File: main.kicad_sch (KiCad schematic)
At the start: 18 parts, among them J1 RPi UART Debug LEDs, J2 mini iso blue, J3 LCD power, P1 Conn_02x20_Odd_Even, U7 DS3231MZ

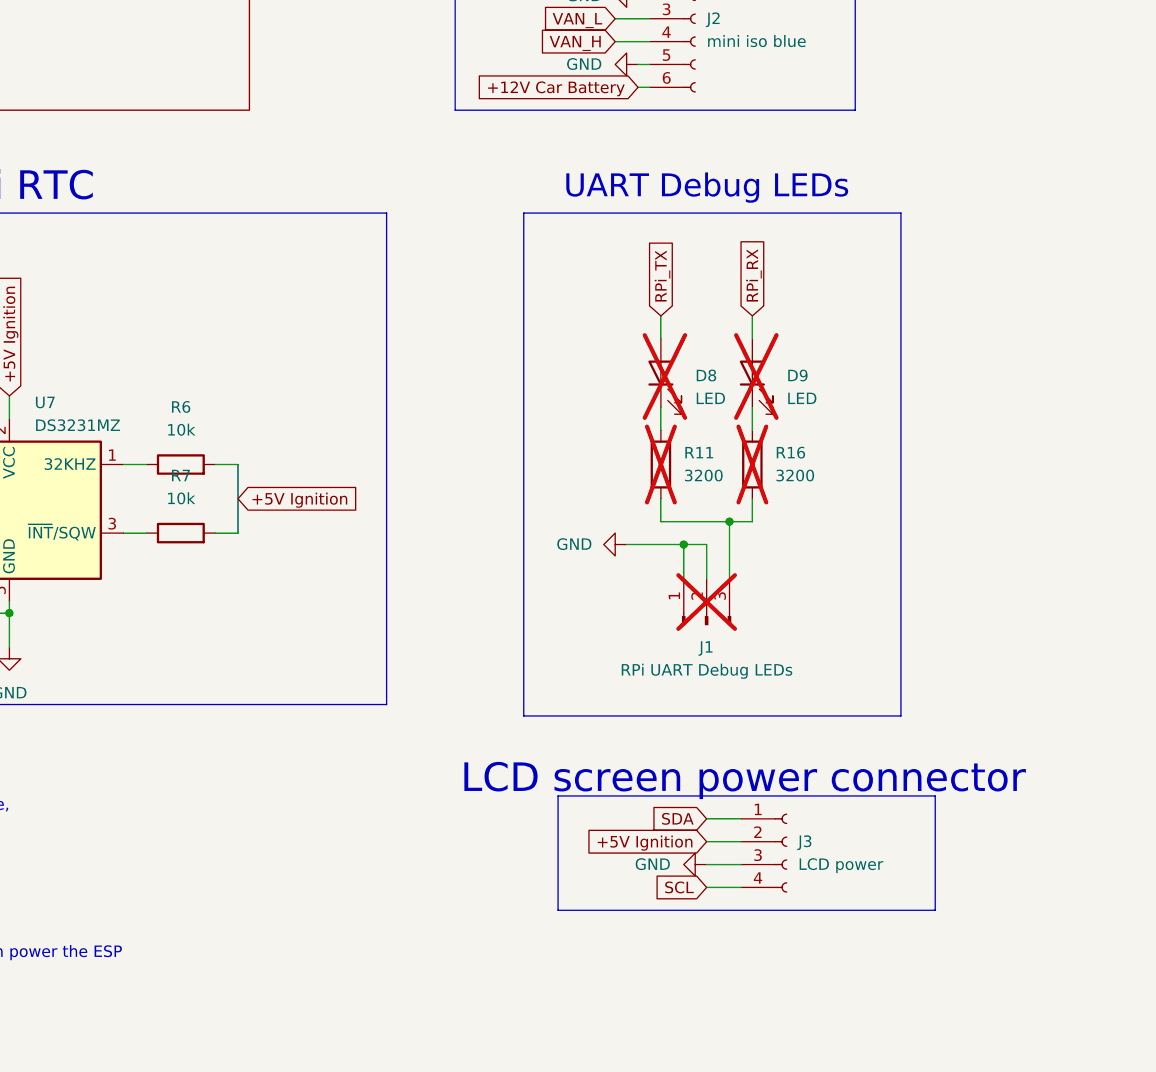
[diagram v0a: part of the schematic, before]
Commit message: implemented the changes from 'Board defects'
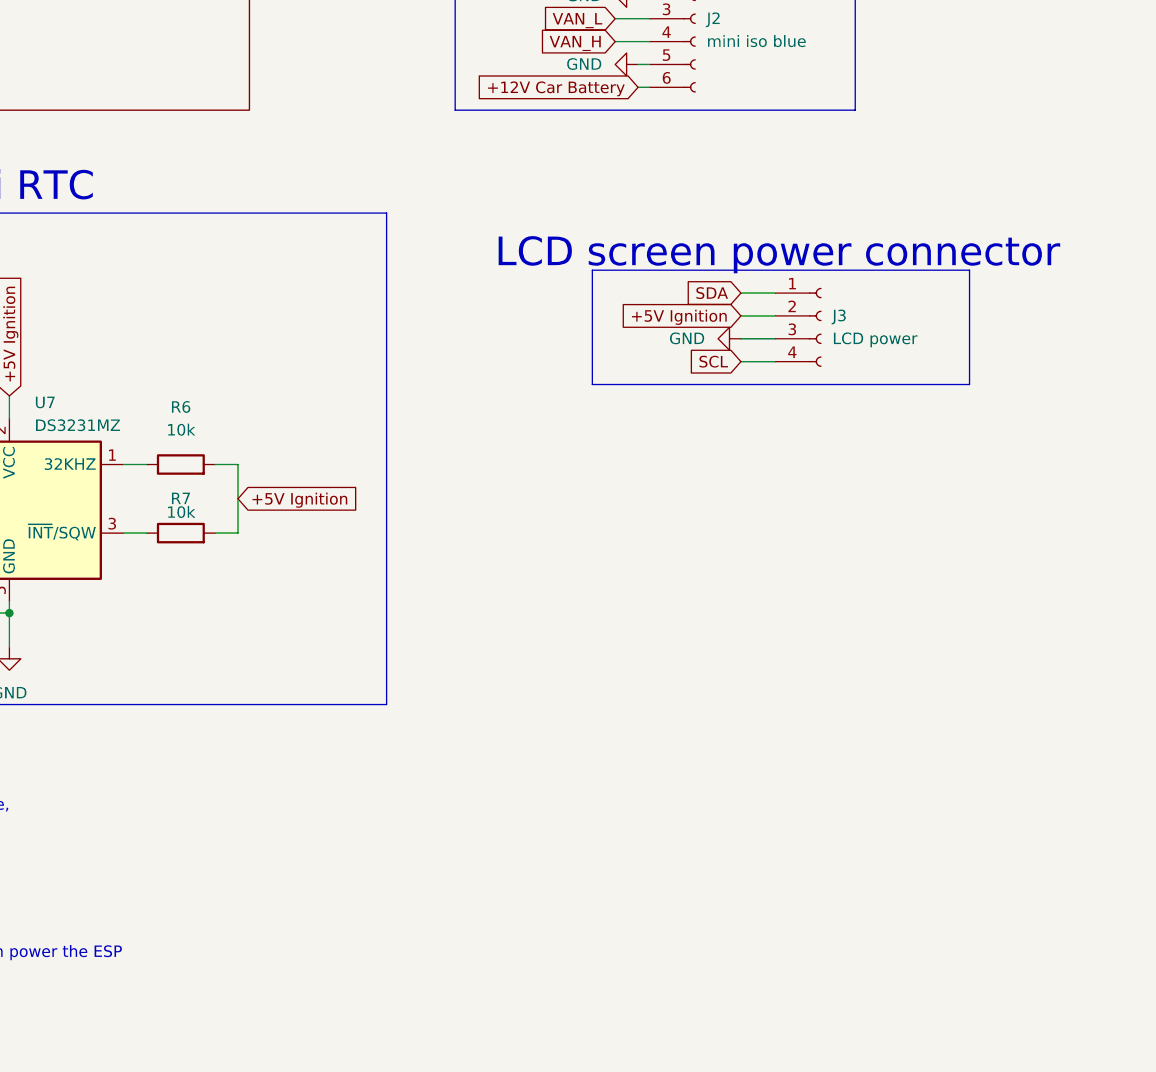
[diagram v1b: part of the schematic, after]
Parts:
- removed D8, D9: LED, LED_SMD:LED_0402_1005Metric, symbol Device:LED
- removed J1: RPi UART Debug LEDs, Connector_PinHeader_2.54mm:PinHeader_1x03_P2.54mm_Vertical, symbol Connector:Conn_01x03_Pin
- removed R11, R16: 3200, Resistor_SMD:R_0805_2012Metric, symbol Device:R
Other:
- note removed: "UART Debug LEDs"
- moved on the sheet: J3

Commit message: 2 layer PCB
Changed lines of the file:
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@@
+	)
+	(junction
+		(at 83.82 88.9)
+		(diameter 1.016)
+		(color 0 0 0 0)
+	)
+	(junction
+		(at 83.82 63.5)
+		(diameter 1.016)
+		(color 0 0 0 0)
+	)
+	(junction
+		(at 66.04 78.74)
+		(diameter 1.016)
+		(color 0 0 0 0)
+	)
+	(junction
+		(at 52.07 53.34)
+		(diameter 0)
+		(color 0 0 0 0)
 	)
 	(junction
@@
 	)
 	(junction
-		(at 83.82 88.9)
-		(diameter 1.016)
-		(color 0 0 0 0)
-	)
-	(junction
-		(at 83.82 63.5)
-		(diameter 1.016)
-		(color 0 0 0 0)
-	)
-	(junction
-		(at 66.04 78.74)
-		(diameter 1.016)
-		(color 0 0 0 0)
-	)
-	(junction
-		(at 52.07 53.34)
-		(diameter 0)
-		(color 0 0 0 0)
-	)
-	(junction
 		(at 123.19 128.27)
 		(diameter 0)
@@
 	(wire
 		(pts
+			(xy 62.23 39.37) (xy 52.07 39.37)
+		)
+		(stroke
+			(width 0)
+			(type default)
+		)
+	)
+	(wire
+		(pts
 			(xy 208.28 67.31) (xy 209.55 67.31)
 		)
@@
 	(wire
 		(pts
+			(xy 52.07 39.37) (xy 52.07 41.91)
+		)
+		(stroke
+			(width 0)
+			(type default)
+		)
+	)
+	(wire
+		(pts
 			(xy 153.67 119.38) (xy 151.13 119.38)
 		)
@@
 	(wire
 		(pts
+			(xy 62.23 48.26) (xy 62.23 63.5)
+		)
+		(stroke
+			(width 0)
+			(type default)
+		)
+	)
+	(wire
+		(pts
 			(xy 83.82 63.5) (xy 81.28 63.5)
 		)
@@
 	(wire
 		(pts
+			(xy 62.23 48.26) (xy 68.58 48.26)
+		)
+		(stroke
+			(width 0)
+			(type default)
+		)
+	)
+	(wire
+		(pts
 			(xy 66.04 78.74) (xy 66.04 96.52)
 		)
@@
 	(wire
 		(pts
-			(xy 52.07 41.91) (xy 62.23 41.91)
-		)
-		(stroke
-			(width 0)
-			(type default)
-		)
-	)
-	(wire
-		(pts
 			(xy 52.07 53.34) (xy 68.58 53.34)
 		)
@@
 	(wire
 		(pts
-			(xy 86.36 44.45) (xy 86.36 48.26)
+			(xy 86.36 33.02) (xy 86.36 48.26)
 		)
 		(stroke
@@
 	(wire
 		(pts
-			(xy 62.23 41.91) (xy 62.23 48.26)
+			(xy 62.23 39.37) (xy 62.23 48.26)
 		)
 		(stroke
@@
 	(wire
 		(pts
-			(xy 62.23 48.26) (xy 68.58 48.26)
-		)
-		(stroke
-			(width 0)
-			(type default)
-		)
-	)
-	(wire
-		(pts
 			(xy 86.36 48.26) (xy 81.28 48.26)
 		)
@@
 		)
 	)
-	(wire
-		(pts
-			(xy 62.23 48.26) (xy 62.23 63.5)
-		)
-		(stroke
-			(width 0)
-			(type default)
-		)
-	)
 	(global_label "+5V Ignition"
 		(shape input)
@@
 	(global_label "+5V Ignition"
 		(shape input)
-		(at 86.36 44.45 90)
+		(at 86.36 33.02 90)
 		(fields_autoplaced yes)
 		(effects
@@
 		)
 		(property "Intersheetrefs" "${INTERSHEET_REFS}"
-			(at 86.36 29.3955 90)
-			(effects
-				(font
+			(at 86.36 17.9655 90)
+			(effects
+				(font

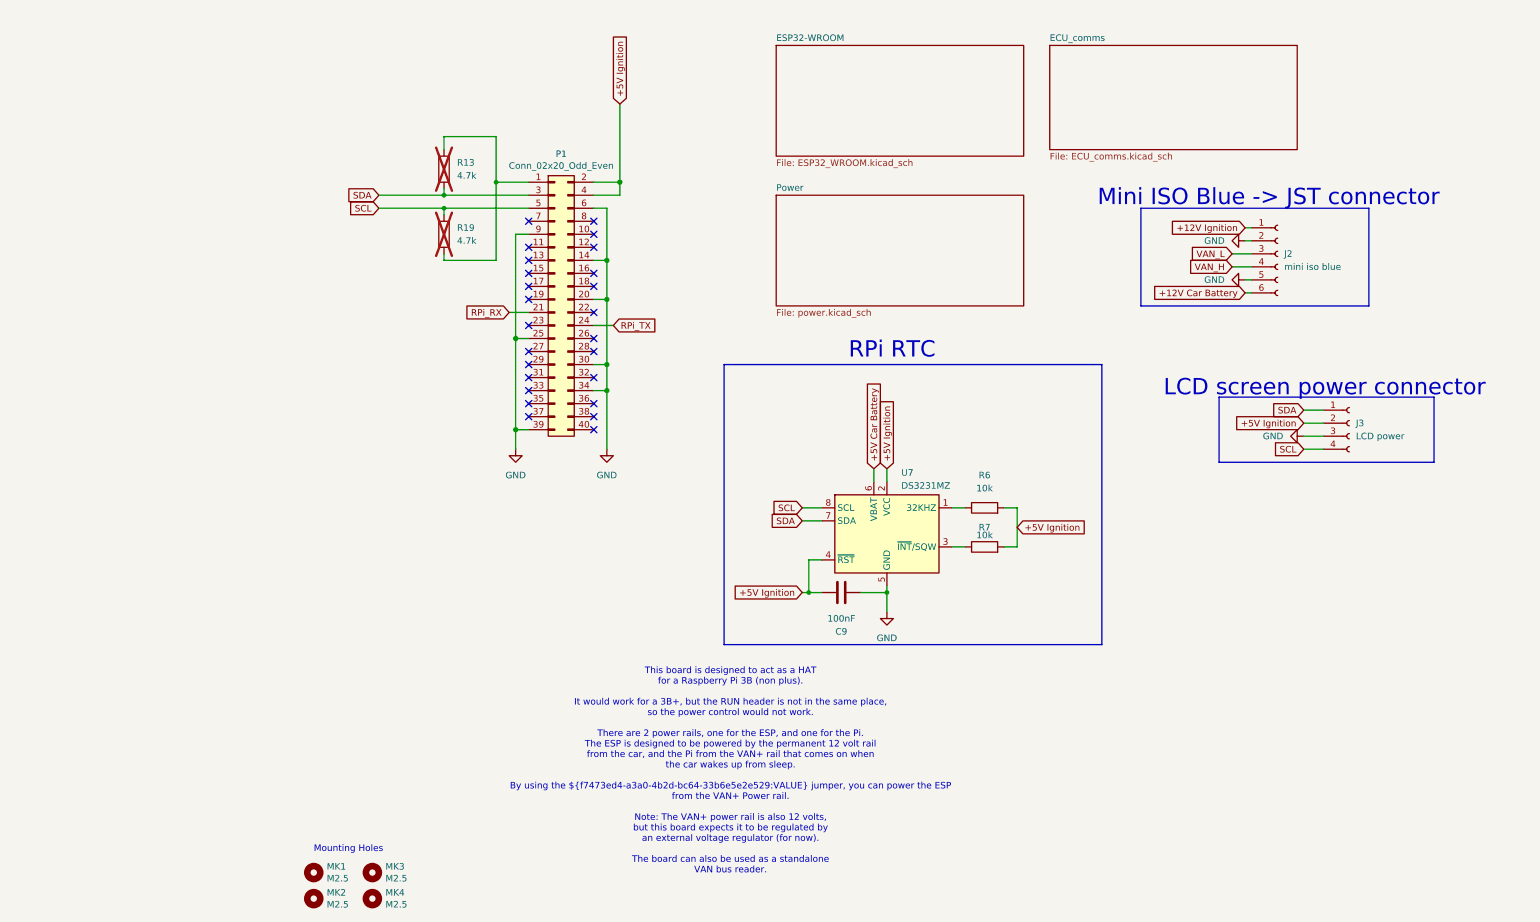
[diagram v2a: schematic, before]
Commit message: Change inductor type.
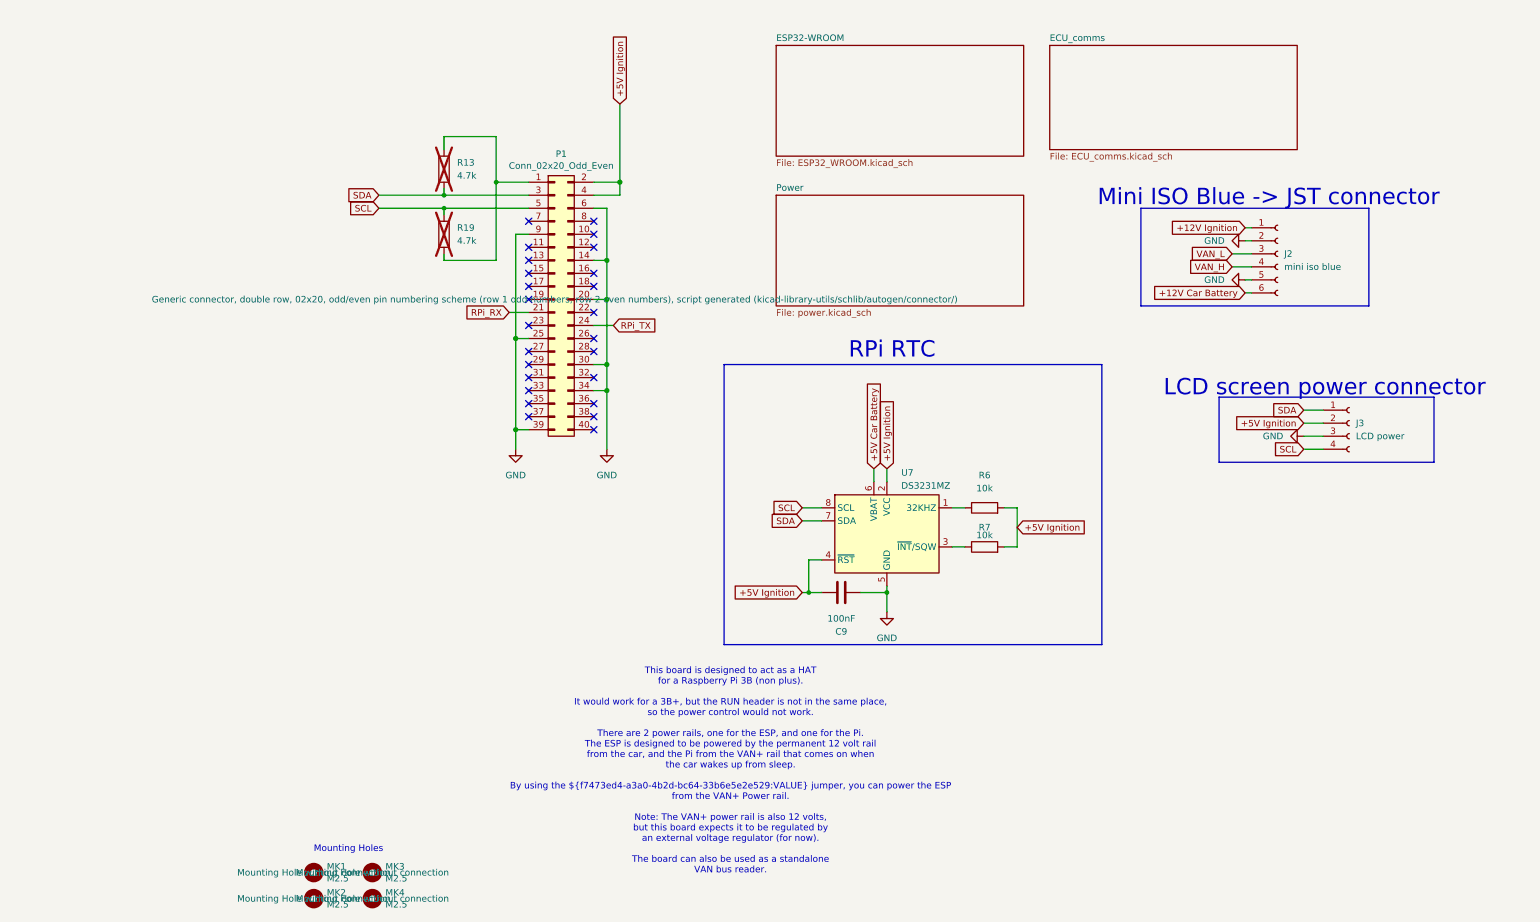
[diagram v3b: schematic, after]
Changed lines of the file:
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@@
 			)
 		)
-		(property "Description" ""
+		(property "Description" "Mounting Hole without connection"
 			(at 26.67 182.88 0)
 			(effects
@@
 			)
 		)
-		(property "Description" ""
+		(property "Description" "Mounting Hole without connection"
 			(at 38.1 182.88 0)
 			(effects
@@
 			)
 		)
-		(property "Description" ""
+		(property "Description" "Mounting Hole without connection"
 			(at 26.67 187.96 0)
 			(effects
@@
 			)
 		)
-		(property "Description" ""
+		(property "Description" "Mounting Hole without connection"
 			(at 38.1 187.96 0)
 			(effects
@@
 			)
 		)
-		(property "Description" ""
+		(property "Description" "Generic connector, double row, 02x20, odd/even pin numbering scheme (row 1 odd numbers, row 2 even numbers), script generated (kicad-library-utils/schlib/autogen/connector/)"
 			(at 73.66 71.12 0)
 			(effects

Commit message: Update bom values with actual chip names
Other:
- note removed: "This board is designed to act as a HAT for a Raspberry Pi 3B (non plus). It would work for a 3B+, but the RUN header is not in the same place, so the power control would not work. There are 2 power rails, one for the ESP, and one for the Pi. The ESP is designed to be powered by the permanent 12 volt rail from the car, and the Pi from the VAN+ rail that comes on when the car wakes up from sleep. B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"
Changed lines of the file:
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@@
-		)
-	)
-	(text "This board is designed to act as a HAT\nfor a Raspberry Pi 3B (non plus).\n\nIt would work for a 3B+, but the RUN header is not in the same place,\nso the power control would not work.\n\nThere are 2 power rails, one for the ESP, and one for the Pi.\nThe ESP is designed to be powered by the permanent 12 volt rail\nfrom the car, and the Pi from the VAN+ rail that comes on when\nthe car wakes up from sleep.\n\nBy using the ${f7473ed4-a3a0-4b2d-bc64-33b6e5e2e529:VALUE} jumper, you can power the ESP\nfrom the VAN+ Power rail.\n\nNote: The VAN+ power rail is also 12 volts, \nbut this board expects it to be regulated by\nan external voltage regulator (for now).\n\nThe board can also be used as a standalone\nVAN bus reader."
-		(exclude_from_sim no)
-		(at 107.95 163.068 0)
-		(effects
-			(font
-				(size 1.27 1.27)
-			)
 		)
 	)
@@
 					(size 1.27 1.27)
 				)
+				(hide yes)
 			)
 		)
@@
 			)
 		)
-		(property "Description" "Unpolarized capacitor"
+		(property "Description" ""
 			(at 129.54 128.27 0)
 			(effects
@@
 			)
 		)
-		(property "Description" "Generic connector, single row, 01x04, script generated"
+		(property "Description" ""
 			(at 228.6 95.25 0)
 			(effects
@@
 			)
 		)
-		(property "Description" "Generic connector, single row, 01x06, script generated"
+		(property "Description" ""
 			(at 214.63 62.23 0)
 			(effects
